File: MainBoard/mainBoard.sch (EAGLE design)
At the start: 121 parts, among them IC1 74HC151D, IC2 LM317, IC3 74HC238, J1 22-05-7038-03, J10 22-05-7038-03, J11 22-05-7038-03, J12 22-05-7038-03, J13 22-05-7038-03, J14 22-05-7038-03, J15 22-05-7038-03, J16 22-05-7038-03, J2 22-05-7038-03, J3 22-05-7038-03, J4 22-05-7038-03, J5 22-05-7038-03, J6 22-05-7038-03, J7 22-05-7038-03, J8 22-05-7038-03, J9 22-05-7038-03, Q1 8MHz, Q10 BC847ASMD, Q12 BC847ASMD, Q2 BC847ASMD, Q4 BC847ASMD, Q6 BC847ASMD, Q8 BC847ASMD, X1 PWR12, X10 MSTBA2, X11 MSTBA2, X12 MSTBA2, X13 MSTBA2, X2 MSTBA2, X3 MSTBA2, X4 MSTBA2, X5 MSTBA2, X6 MSTBA2, X7 MSTBA2, X8 MSTBA2, X9 MSTBA2

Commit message: mainboard updates
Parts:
- added C18: 4.7u/35V, rcl:CPOL-EUB
- added C19: 10n, rcl:C-EUC0603K
- added C2, C20: 100n, rcl:C-EUC0603K
- added IC4: FT232RL, ftdichip:FT232RL
- added J19: J7MM, jumper:J7MM
- added R37, R38: EMI 60Ohm Ferrit, rcl:R-EU_R0603
- added SJ1: (no value), jumper:SJ
- added X15: MINI-USB-SCHIELD-32005-301, con-cypressindustries:MINI-USB-SCHIELD-32005-301
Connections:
- new net DM: IC4.USBDM, X15G$1.2
- new net DP: IC4.USBDP, X15G$1.3
- new net ID: X15G$1.4
- new net N$27: R38.2, SJ1.2, X15S.S3
- new net N$32: C20.1, IC4.3V3OUT
- new net PB0: R17.1, U$1.PB0
- new net PB10: R21.1, U$1.PB10
- new net VBUS: C19.1, R37.1, X15G$1.1
- new net VCCUSB: C18.+, C2.1, IC4.VCC, IC4.VCCIO, R37.2
- net +3V3: now also J19.1, J19.2, S2.S1, S3.S1, S4.S1
- net GND: now also C18.-, C19.2, C2.2, C20.2, IC4.GND, IC4.GND@1, IC4.GND@2, IC4.GND@A, R38.1, SJ1.1, X15G$1.5
- net PA4: now also R2.1; no longer R13.1
- net PA5: no longer R17.1
- net PA6: now also R9.1; no longer R21.1
- net PA7: now also R13.1; no longer R26.1
- net PA8: now also R26.1
- net PF4: no longer R2.1
- net PF5: no longer R9.1
- net USART1_RX: now also IC4.TXD
- net USART1_TX: now also IC4.RXD

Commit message: mainboard updates
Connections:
- net GND renamed GND123
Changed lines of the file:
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@@
 <grid distance="0.1" unitdist="inch" unit="inch" style="lines" multiple="1" display="no" altdistance="0.01" altunitdist="inch" altunit="inch"/>
 <layers>
-<layer number="1" name="Top" color="4" fill="1" visible="yes" active="no"/>
-<layer number="2" name="Route2" color="1" fill="3" visible="yes" active="no"/>
-<layer number="3" name="Route3" color="4" fill="3" visible="yes" active="no"/>
-<layer number="4" name="Route4" color="1" fill="4" visible="yes" active="no"/>
-<layer number="5" name="Route5" color="4" fill="4" visible="yes" active="no"/>
-<layer number="6" name="Route6" color="1" fill="8" visible="yes" active="no"/>
-<layer number="7" name="Route7" color="4" fill="8" visible="yes" active="no"/>
-<layer number="8" name="Route8" color="1" fill="2" visible="yes" active="no"/>
-<layer number="9" name="Route9" color="4" fill="2" visible="yes" active="no"/>
-<layer number="10" name="Route10" color="1" fill="7" visible="yes" active="no"/>
-<layer number="11" name="Route11" color="4" fill="7" visible="yes" active="no"/>
-<layer number="12" name="Route12" color="1" fill="5" visible="yes" active="no"/>
-<layer number="13" name="Route13" color="4" fill="5" visible="yes" active="no"/>
-<layer number="14" name="Route14" color="1" fill="6" visible="yes" active="no"/>
-<layer number="15" name="Route15" color="4" fill="6" visible="yes" active="no"/>
-<layer number="16" name="Bottom" color="1" fill="1" visible="yes" active="no"/>
-<layer number="17" name="Pads" color="2" fill="1" visible="yes" active="no"/>
-<layer number="18" name="Vias" color="2" fill="1" visible="yes" active="no"/>
-<layer number="19" name="Unrouted" color="6" fill="1" visible="yes" active="no"/>
-<layer number="20" name="Dimension" color="15" fill="1" visible="yes" active="no"/>
-<layer number="21" name="tPlace" color="7" fill="1" visible="yes" active="no"/>
-<layer number="22" name="bPlace" color="7" fill="1" visible="yes" active="no"/>
-<layer number="23" name="tOrigins" color="15" fill="1" visible="yes" active="no"/>
-<layer number="24" name="bOrigins" color="15" fill="1" visible="yes" active="no"/>
-<layer number="25" name="tNames" color="7" fill="1" visible="yes" active="no"/>
-<layer number="26" name="bNames" color="7" fill="1" visible="yes" active="no"/>
-<layer number="27" name="tValues" color="7" fill="1" visible="yes" active="no"/>
-<layer number="28" name="bValues" color="7" fill="1" visible="yes" active="no"/>
+<layer number="1" name="Top" color="4" fill="1" visible="no" active="no"/>
+<layer number="2" name="Route2" color="1" fill="3" visible="no" active="no"/>
+<layer number="3" name="Route3" color="4" fill="3" visible="no" active="no"/>
+<layer number="4" name="Route4" color="1" fill="4" visible="no" active="no"/>
+<layer number="5" name="Route5" color="4" fill="4" visible="no" active="no"/>
+<layer number="6" name="Route6" color="1" fill="8" visible="no" active="no"/>
+<layer number="7" name="Route7" color="4" fill="8" visible="no" active="no"/>
+<layer number="8" name="Route8" color="1" fill="2" visible="no" active="no"/>
+<layer number="9" name="Route9" color="4" fill="2" visible="no" active="no"/>
+<layer number="10" name="Route10" color="1" fill="7" visible="no" active="no"/>
+<layer number="11" name="Route11" color="4" fill="7" visible="no" active="no"/>
+<layer number="12" name="Route12" color="1" fill="5" visible="no" active="no"/>
+<layer number="13" name="Route13" color="4" fill="5" visible="no" active="no"/>
+<layer number="14" name="Route14" color="1" fill="6" visible="no" active="no"/>
+<layer number="15" name="Route15" color="4" fill="6" visible="no" active="no"/>
+<layer number="16" name="Bottom" color="1" fill="1" visible="no" active="no"/>
+<layer number="17" name="Pads" color="2" fill="1" visible="no" active="no"/>
+<layer number="18" name="Vias" color="2" fill="1" visible="no" active="no"/>
+<layer number="19" name="Unrouted" color="6" fill="1" visible="no" active="no"/>
+<layer number="20" name="Dimension" color="15" fill="1" visible="no" active="no"/>
+<layer number="21" name="tPlace" color="7" fill="1" visible="no" active="no"/>
+<layer number="22" name="bPlace" color="7" fill="1" visible="no" active="no"/>
+<layer number="23" name="tOrigins" color="15" fill="1" visible="no" active="no"/>
+<layer number="24" name="bOrigins" color="15" fill="1" visible="no" active="no"/>
+<layer number="25" name="tNames" color="7" fill="1" visible="no" active="no"/>
+<layer number="26" name="bNames" color="7" fill="1" visible="no" active="no"/>
+<layer number="27" name="tValues" color="7" fill="1" visible="no" active="no"/>
+<layer number="28" name="bValues" color="7" fill="1" visible="no" active="no"/>
 <layer number="29" name="tStop" color="7" fill="3" visible="no" active="no"/>
 <layer number="30" name="bStop" color="7" fill="6" visible="no" active="no"/>
@@
 <layer number="35" name="tGlue" color="7" fill="4" visible="no" active="no"/>
 <layer number="36" name="bGlue" color="7" fill="5" visible="no" active="no"/>
-<layer number="37" name="tTest" color="7" fill="1" visible="yes" active="no"/>
-<layer number="38" name="bTest" color="7" fill="1" visible="yes" active="no"/>
+<layer number="37" name="tTest" color="7" fill="1" visible="no" active="no"/>
+<layer number="38" name="bTest" color="7" fill="1" visible="no" active="no"/>
 <layer number="39" name="tKeepout" color="4" fill="11" visible="no" active="no"/>
 <layer number="40" name="bKeepout" color="1" fill="11" visible="no" active="no"/>
@@
 <layer number="44" name="Drills" color="7" fill="1" visible="no" active="no"/>
 <layer number="45" name="Holes" color="7" fill="1" visible="no" active="no"/>
-<layer number="46" name="Milling" color="3" fill="1" visible="yes" active="no"/>
-<layer number="47" name="Measures" color="7" fill="1" visible="yes" active="no"/>
-<layer number="48" name="Document" color="7" fill="1" visible="yes" active="no"/>
-<layer number="49" name="Reference" color="7" fill="1" visible="yes" active="no"/>
-<layer number="51" name="tDocu" color="7" fill="1" visible="yes" active="no"/>
-<layer number="52" name="bDocu" color="7" fill="1" visible="yes" active="no"/>
+<layer number="46" name="Milling" color="3" fill="1" visible="no" active="no"/>
+<layer number="47" name="Measures" color="7" fill="1" visible="no" active="no"/>
+<layer number="48" name="Document" color="7" fill="1" visible="no" active="no"/>
+<layer number="49" name="Reference" color="7" fill="1" visible="no" active="no"/>
+<layer number="51" name="tDocu" color="7" fill="1" visible="no" active="no"/>
+<layer number="52" name="bDocu" color="7" fill="1" visible="no" active="no"/>
 <layer number="91" name="Nets" color="2" fill="1" visible="yes" active="yes"/>
 <layer number="92" name="Busses" color="1" fill="1" visible="yes" active="yes"/>
@@
 </segment>
 </net>
-<net name="GND" class="0">
+<net name="GND123" class="0">
 <segment>
 <pinref part="JP3" gate="A" pin="4"/>
@@
 </busses>
 <nets>
-<net name="GND" class="0">
+<net name="GND123" class="0">
 <segment>
 <pinref part="C9" gate="G$1" pin="2"/>
@@
 </segment>
 </net>
-<net name="GND" class="0">
+<net name="GND123" class="0">
 <segment>
 <pinref part="IC3" gate="P" pin="GND"/>
@@
 </segment>
 </net>
-<net name="GND" class="0">
+<net name="GND123" class="0">
 <segment>
 <pinref part="GND36" gate="1" pin="GND"/>
@@
 </segment>
 </net>
-<net name="GND" class="0">
+<net name="GND123" class="0">
 <segment>
 <pinref part="R4" gate="G$1" pin="1"/>

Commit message: fw updates and docu
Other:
- note added: "CPU / Main"
- note added: "Motor Control"
- note added: "Other Things"
- note added: "Power Supply"
- note added: "Sensors"
- note added: "User Interface"
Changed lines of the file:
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@@
 <description>CPU</description>
 <plain>
+<text x="162.56" y="20.32" size="2.54" layer="91">CPU / Main</text>
 </plain>
 <instances>
@@
 <description>PowerSupply</description>
 <plain>
+<text x="162.56" y="20.32" size="2.54" layer="91">Power Supply</text>
 </plain>
 <instances>
@@
 <text x="182.88" y="165.1" size="1.778" layer="91">Stecker:
 Reichelt 8x PSK 254/3W</text>
+<text x="162.56" y="20.32" size="2.54" layer="91">Sensors</text>
 </plain>
 <instances>
@@
 <description>UserInterface</description>
 <plain>
+<text x="162.56" y="20.32" size="2.54" layer="91">User Interface</text>
 </plain>
 <instances>
@@
 <description>Pumps</description>
 <plain>
+<text x="162.56" y="20.32" size="2.54" layer="91">Motor Control</text>
 </plain>
 <instances>
@@
 <description>OtherThings</description>
 <plain>
+<text x="162.56" y="20.32" size="2.54" layer="91">Other Things</text>
 </plain>
 <instances>

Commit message: mainboard updates
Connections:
- removed net D_SCLK_SCL: SV5.5
- removed net D_SID_SDAIN: SV5.6
- removed net D_SOD_SDAOUT: SV5.7
- removed net PB3: U$1.PB3
- removed net PF4: U$1.PF4
- removed net PF5: U$1.PF5
- new net SPI1_MISO: SV5.7, U$1.PB4
- new net SPI1_MOSI: SV5.6, U$1.PB5
- new net SPI1_SCK: SV5.5, U$1.PB3
- net D_IM1: now also U$1.PF4
- net D_IM2: now also U$1.PF5
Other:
- note added: "connectors:"
- note added: "display:"
- note removed: "Stecker: Reichelt 8x PSK 254/3W"
- moved on the sheet: X10-1, X10-2, X11-1, X11-2, X12-1, X12-2, X13-1, X13-2, X2-1, X2-2, X3-1, X3-2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

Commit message: mainboard updates
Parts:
- added LED2: (no value), led:LED3MM
- added R39: 100, rcl:R-EU_R0805
- J19: value J7MM -> J5MM; device jumper:J7MM -> jumper:J5MM
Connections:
- removed net GND123: C1.-, C10.2, C11.-, C18.-, C19.2, C2.2, C20.2, C3.2, C4.2, C5.2, C6.2, C7.2, C8.2, C9.2, D1.A, D2.A, D3.A, D4.A, D5.A, D6.A, IC1P.GND, IC3P.GND, IC4.GND, IC4.GND@1, IC4.GND@2, IC4.GND@A, J1-3.S, J10-3.S, J11-3.S, J12-3.S, J13-3.S, J14-3.S, J15-3.S, J16-3.S, J2-3.S, J3-3.S, J4-3.S, J5-3.S, J6-3.S, J7-3.S, J8-3.S, J9-3.S, JP1.3, JP3.4, Q10.E, Q12.E, Q2.E, Q4.E, Q6.E, Q8.E, R1.1, R10.1, R14.1, R18.1, R22.1, R27.1, R3.2, R32.1, R33.1, R34.1, R35.1, R36.1, R38.1, R4.1, SJ1.1, SV1.7, SV3.1, SV3.2, SV3.3, SV4.1, U$1.BOOT0, U$1.VSSA, U$1.VSS_1, U$1.VSS_2, X1-2.KL, X10-2.1, X11-2.1, X12-2.1, X13-2.1, X15G$1.5, X2-2.1, X3-2.1, X4-2.1, X5-2.1, X6-2.1, X7-2.1, X8-2.1, X9-2.1
- new net ERROR_LED: LED2.A, U$1.PC13
- new net GND: C1.-, C10.2, C11.-, C18.-, C19.2, C2.2, C20.2, C3.2, C4.2, C5.2, C6.2, C7.2, C8.2, C9.2, D1.A, D2.A, D3.A, D4.A, D5.A, D6.A, IC1P.GND, IC3P.GND, IC4.GND, IC4.GND@1, IC4.GND@2, IC4.GND@A, J1-3.S, J10-3.S, J11-3.S, J12-3.S, J13-3.S, J14-3.S, J15-3.S, J16-3.S, J2-3.S, J3-3.S, J4-3.S, J5-3.S, J6-3.S, J7-3.S, J8-3.S, J9-3.S, JP1.3, JP3.4, Q10.E, Q12.E, Q2.E, Q4.E, Q6.E, Q8.E, R1.1, R10.1, R14.1, R18.1, R22.1, R27.1, R3.2, R32.1, R33.1, R34.1, R35.1, R36.1, R38.1, R39.1, R4.1, SJ1.1, SV1.7, SV3.1, SV3.2, SV3.3, SV4.1, U$1.BOOT0, U$1.VSSA, U$1.VSS_1, U$1.VSS_2, X1-2.KL, X10-2.1, X11-2.1, X12-2.1, X13-2.1, X15G$1.5, X2-2.1, X3-2.1, X4-2.1, X5-2.1, X6-2.1, X7-2.1, X8-2.1, X9-2.1
- new net N$29: LED2.C, R39.2
- net D_ENABLE: now also U$1.PC9
- net D_RESET: now also U$1.PC6
- net D_RS: now also U$1.PC7
- net D_RW: now also U$1.PC8

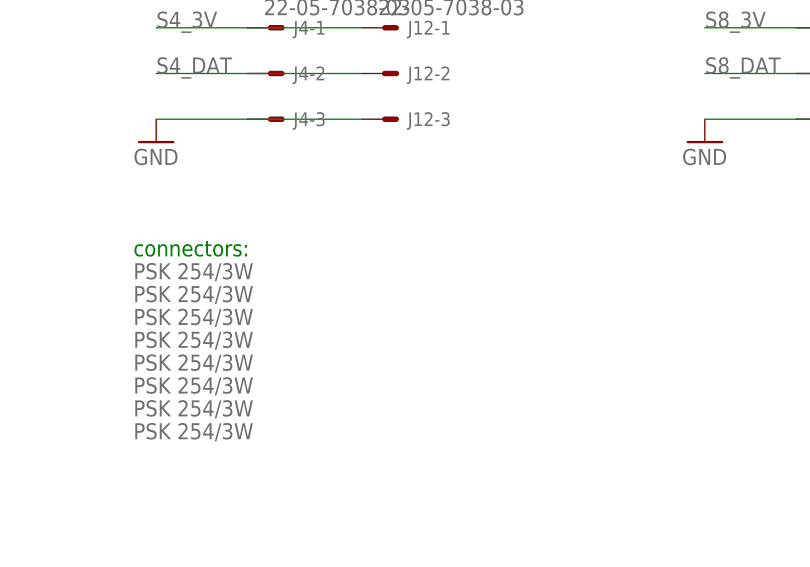
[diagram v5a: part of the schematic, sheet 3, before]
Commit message: fix BOM generation; some board fixes
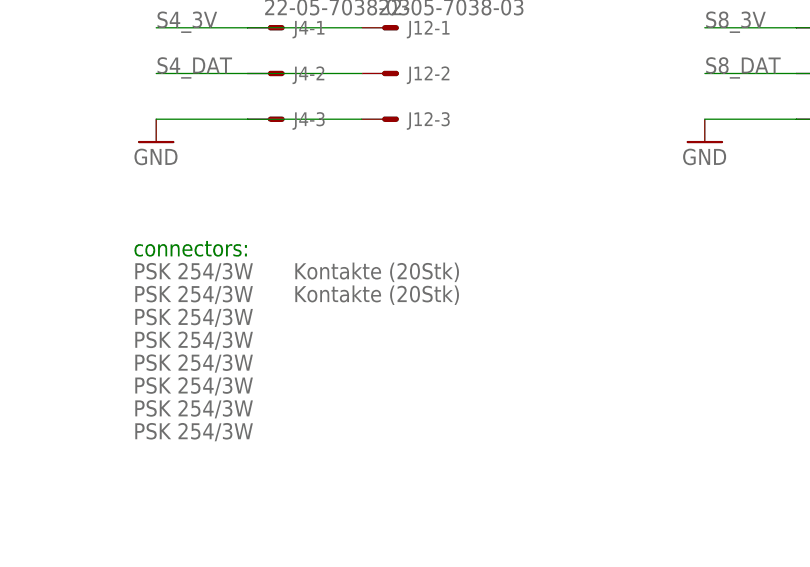
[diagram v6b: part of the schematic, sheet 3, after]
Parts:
- added U$10, U$3, U$4, U$5, U$6, U$7, U$8, U$9: PSK 254/3W, extra:DUMMY_BOM
- added U$11: EA DOGM204W-A, extra:DUMMY_BOM
- added U$12, U$13, U$14, U$15, U$16, U$17: AKL 249-02, extra:DUMMY_BOM
- added U$18, U$19: Kontakte (20Stk), extra:DUMMY_BOM
- C1, C11: device rcl:CPOL-EUG -> rcl:CPOL-EUD
- D1, D2, D3, D4, D5, D6: device diode:SCHOTTKY-DIODESMD -> diode:SCHOTTKY-DIODESMC
- Q10, Q12, Q2, Q4, Q6, Q8: R BC 547A -> BC 847A SMD

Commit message: mainboard updates
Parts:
- removed J19: J5MM, jumper:J5MM
- U$3: BOM (none) -> yes
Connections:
- net +3V3: no longer J19.1, J19.2
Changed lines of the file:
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@@
 <grid distance="0.1" unitdist="inch" unit="inch" style="lines" multiple="1" display="no" altdistance="0.01" altunitdist="inch" altunit="inch"/>
 <layers>
-<layer number="1" name="Top" color="4" fill="1" visible="yes" active="no"/>
-<layer number="2" name="Route2" color="1" fill="3" visible="yes" active="no"/>
-<layer number="3" name="Route3" color="4" fill="3" visible="yes" active="no"/>
-<layer number="4" name="Route4" color="1" fill="4" visible="yes" active="no"/>
-<layer number="5" name="Route5" color="4" fill="4" visible="yes" active="no"/>
-<layer number="6" name="Route6" color="1" fill="8" visible="yes" active="no"/>
-<layer number="7" name="Route7" color="4" fill="8" visible="yes" active="no"/>
-<layer number="8" name="Route8" color="1" fill="2" visible="yes" active="no"/>
-<layer number="9" name="Route9" color="4" fill="2" visible="yes" active="no"/>
-<layer number="10" name="Route10" color="1" fill="7" visible="yes" active="no"/>
-<layer number="11" name="Route11" color="4" fill="7" visible="yes" active="no"/>
-<layer number="12" name="Route12" color="1" fill="5" visible="yes" active="no"/>
-<layer number="13" name="Route13" color="4" fill="5" visible="yes" active="no"/>
-<layer number="14" name="Route14" color="1" fill="6" visible="yes" active="no"/>
-<layer number="15" name="Route15" color="4" fill="6" visible="yes" active="no"/>
-<layer number="16" name="Bottom" color="1" fill="1" visible="yes" active="no"/>
-<layer number="17" name="Pads" color="2" fill="1" visible="yes" active="no"/>
-<layer number="18" name="Vias" color="2" fill="1" visible="yes" active="no"/>
-<layer number="19" name="Unrouted" color="6" fill="1" visible="yes" active="no"/>
-<layer number="20" name="Dimension" color="15" fill="1" visible="yes" active="no"/>
-<layer number="21" name="tPlace" color="7" fill="1" visible="yes" active="no"/>
-<layer number="22" name="bPlace" color="7" fill="1" visible="yes" active="no"/>
-<layer number="23" name="tOrigins" color="15" fill="1" visible="yes" active="no"/>
-<layer number="24" name="bOrigins" color="15" fill="1" visible="yes" active="no"/>
-<layer number="25" name="tNames" color="7" fill="1" visible="yes" active="no"/>
-<layer number="26" name="bNames" color="7" fill="1" visible="yes" active="no"/>
-<layer number="27" name="tValues" color="7" fill="1" visible="yes" active="no"/>
-<layer number="28" name="bValues" color="7" fill="1" visible="yes" active="no"/>
+<layer number="1" name="Top" color="4" fill="1" visible="no" active="no"/>
+<layer number="2" name="Route2" color="1" fill="3" visible="no" active="no"/>
+<layer number="3" name="Route3" color="4" fill="3" visible="no" active="no"/>
+<layer number="4" name="Route4" color="1" fill="4" visible="no" active="no"/>
+<layer number="5" name="Route5" color="4" fill="4" visible="no" active="no"/>
+<layer number="6" name="Route6" color="1" fill="8" visible="no" active="no"/>
+<layer number="7" name="Route7" color="4" fill="8" visible="no" active="no"/>
+<layer number="8" name="Route8" color="1" fill="2" visible="no" active="no"/>
+<layer number="9" name="Route9" color="4" fill="2" visible="no" active="no"/>
+<layer number="10" name="Route10" color="1" fill="7" visible="no" active="no"/>
+<layer number="11" name="Route11" color="4" fill="7" visible="no" active="no"/>
+<layer number="12" name="Route12" color="1" fill="5" visible="no" active="no"/>
+<layer number="13" name="Route13" color="4" fill="5" visible="no" active="no"/>
+<layer number="14" name="Route14" color="1" fill="6" visible="no" active="no"/>
+<layer number="15" name="Route15" color="4" fill="6" visible="no" active="no"/>
+<layer number="16" name="Bottom" color="1" fill="1" visible="no" active="no"/>
+<layer number="17" name="Pads" color="2" fill="1" visible="no" active="no"/>
+<layer number="18" name="Vias" color="2" fill="1" visible="no" active="no"/>
+<layer number="19" name="Unrouted" color="6" fill="1" visible="no" active="no"/>
+<layer number="20" name="Dimension" color="15" fill="1" visible="no" active="no"/>
+<layer number="21" name="tPlace" color="7" fill="1" visible="no" active="no"/>
+<layer number="22" name="bPlace" color="7" fill="1" visible="no" active="no"/>
+<layer number="23" name="tOrigins" color="15" fill="1" visible="no" active="no"/>
+<layer number="24" name="bOrigins" color="15" fill="1" visible="no" active="no"/>
+<layer number="25" name="tNames" color="7" fill="1" visible="no" active="no"/>
+<layer number="26" name="bNames" color="7" fill="1" visible="no" active="no"/>
+<layer number="27" name="tValues" color="7" fill="1" visible="no" active="no"/>
+<layer number="28" name="bValues" color="7" fill="1" visible="no" active="no"/>
 <layer number="29" name="tStop" color="7" fill="3" visible="no" active="no"/>
 <layer number="30" name="bStop" color="7" fill="6" visible="no" active="no"/>
@@
 <layer number="35" name="tGlue" color="7" fill="4" visible="no" active="no"/>
 <layer number="36" name="bGlue" color="7" fill="5" visible="no" active="no"/>
-<layer number="37" name="tTest" color="7" fill="1" visible="yes" active="no"/>
-<layer number="38" name="bTest" color="7" fill="1" visible="yes" active="no"/>
+<layer number="37" name="tTest" color="7" fill="1" visible="no" active="no"/>
+<layer number="38" name="bTest" color="7" fill="1" visible="no" active="no"/>
 <layer number="39" name="tKeepout" color="4" fill="11" visible="no" active="no"/>
 <layer number="40" name="bKeepout" color="1" fill="11" visible="no" active="no"/>
@@
 <layer number="44" name="Drills" color="7" fill="1" visible="no" active="no"/>
 <layer number="45" name="Holes" color="7" fill="1" visible="no" active="no"/>
-<layer number="46" name="Milling" color="3" fill="1" visible="yes" active="no"/>
-<layer number="47" name="Measures" color="7" fill="1" visible="yes" active="no"/>
-<layer number="48" name="Document" color="7" fill="1" visible="yes" active="no"/>
-<layer number="49" name="Reference" color="7" fill="1" visible="yes" active="no"/>
-<layer number="51" name="tDocu" color="7" fill="1" visible="yes" active="no"/>
-<layer number="52" name="bDocu" color="7" fill="1" visible="yes" active="no"/>
+<layer number="46" name="Milling" color="3" fill="1" visible="no" active="no"/>
+<layer number="47" name="Measures" color="7" fill="1" visible="no" active="no"/>
+<layer number="48" name="Document" color="7" fill="1" visible="no" active="no"/>
+<layer number="49" name="Reference" color="7" fill="1" visible="no" active="no"/>
+<layer number="51" name="tDocu" color="7" fill="1" visible="no" active="no"/>
+<layer number="52" name="bDocu" color="7" fill="1" visible="no" active="no"/>
 <layer number="91" name="Nets" color="2" fill="1" visible="yes" active="yes"/>
 <layer number="92" name="Busses" color="1" fill="1" visible="yes" active="yes"/>
@@
 </part>
 <part name="SJ1" library="jumper" deviceset="SJ" device=""/>
-<part name="J19" library="jumper" deviceset="J" device="5MM" value="J5MM"/>
-<part name="+3V19" library="supply1" deviceset="+3V3" device=""/>
-<part name="+3V20" library="supply1" deviceset="+3V3" device=""/>
 <part name="C19" library="rcl" deviceset="C-EU" device="C0603K" value="10n">
 <attribute name="R" value="X7R-G0603 10N"/>
@@
 <part name="GND50" library="supply1" deviceset="GND" device=""/>
 <part name="U$3" library="extra" deviceset="DUMMY_BOM" device="" value="PSK 254/3W">
+<attribute name="BOM" value="yes"/>
 <attribute name="R" value="PSK 254/3W"/>
 </part>
@@
 <instance part="GND11" gate="1" x="88.9" y="121.92"/>
 <instance part="FRAME4" gate="G$1" x="0" y="0"/>
-<instance part="J19" gate="1" x="73.66" y="93.98"/>
-<instance part="+3V19" gate="G$1" x="63.5" y="99.06"/>
-<instance part="+3V20" gate="G$1" x="83.82" y="99.06"/>
 </instances>
 <busses>
@@
 <pinref part="LED1" gate="G$1" pin="A"/>
 <wire x1="187.96" y1="154.94" x2="187.96" y2="152.4" width="0.1524" layer="91"/>
-</segment>
-<segment>
-<pinref part="+3V19" gate="G$1" pin="+3V3"/>
-<wire x1="63.5" y1="96.52" x2="63.5" y2="93.98" width="0.1524" layer="91"/>
-<pinref part="J19" gate="1" pin="1"/>
-<wire x1="63.5" y1="93.98" x2="68.58" y2="93.98" width="0.1524" layer="91"/>
-</segment>
-<segment>
-<pinref part="J19" gate="1" pin="2"/>
-<pinref part="+3V20" gate="G$1" pin="+3V3"/>
-<wire x1="78.74" y1="93.98" x2="83.82" y2="93.98" width="0.1524" layer="91"/>
-<wire x1="83.82" y1="93.98" x2="83.82" y2="96.52" width="0.1524" layer="91"/>
 </segment>
 </net>
@@
 <instance part="U$3" gate="G$1" x="129.54" y="66.04">
 <attribute name="R" x="129.54" y="66.04" size="1.778" layer="96" display="off"/>
+<attribute name="BOM" x="129.54" y="66.04" size="1.778" layer="96" display="off"/>
 </instance>
 <instance part="U$4" gate="G$1" x="129.54" y="63.5">
